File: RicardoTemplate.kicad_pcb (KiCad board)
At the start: 4 copper layers, 42.8 x 63.6 mm, 137 parts, among them IC2 SX1280, J1 RBUS, J2 USB_C_Receptacle_USB2.0, U1 ESP32-S3, U11 SC4215ASTRT, U12 SKY66112-11, U13 DEA202450BT-1213C1, U2 SN65HVD230, U3 LM66200DRLR, U4 MAX77827AEFD+T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

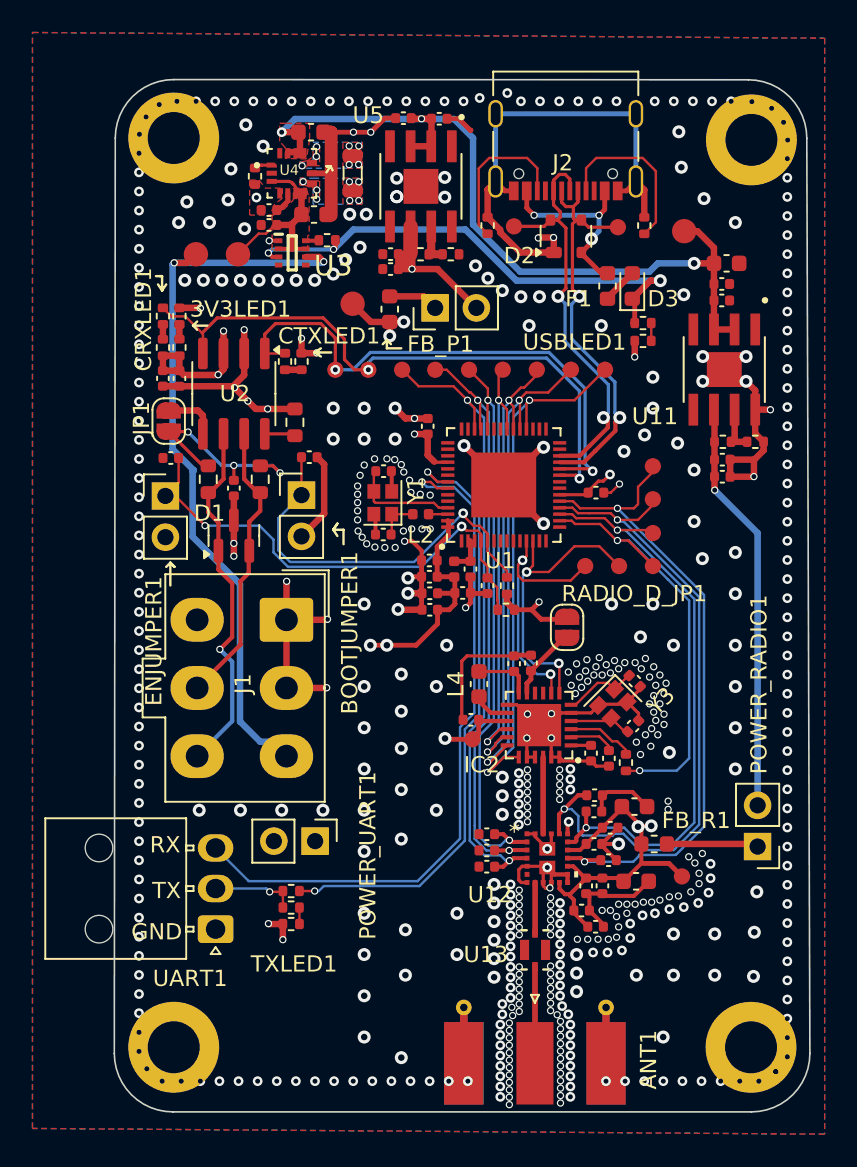
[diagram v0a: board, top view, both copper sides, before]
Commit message: Changed via stitching
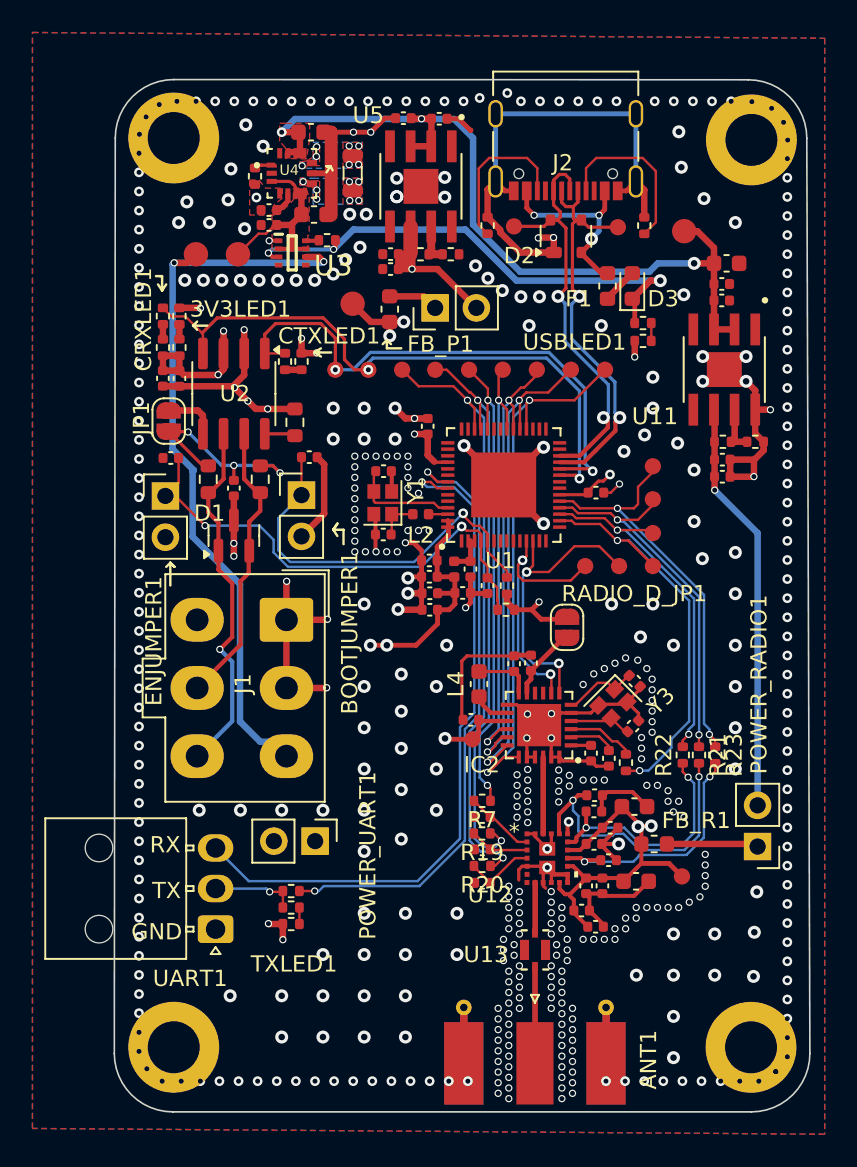
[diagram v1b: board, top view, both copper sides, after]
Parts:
- added R19: 1k, Resistor_SMD:R_0402_1005Metric, F.Cu at (141.1, 117.4)
- added R20: 1k, Resistor_SMD:R_0402_1005Metric, F.Cu at (141.1, 119.4)
- added R21: 1k, Resistor_SMD:R_0402_1005Metric, F.Cu at (154.5, 112.6)
- added R22: 1k, Resistor_SMD:R_0402_1005Metric, F.Cu at (153.5, 112.6)
- added R23: 1k, Resistor_SMD:R_0402_1005Metric, F.Cu at (155.5, 112.6)
- added R7: 1k, Resistor_SMD:R_0402_1005Metric, F.Cu at (141.1, 115.4)
- moved C59 1.09 mm to (141.1, 116.4)
- moved C63 1.03 mm to (141.1, 120.5)
- moved C60 0.28 mm to (141.1, 118.4)
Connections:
- C59 pad 1: CRX -> Net-(U12-CRX)
- C60 pad 1: CSD -> Net-(U12-CSD)
- C63 pad 1: ANT_SEL -> Net-(U12-ANT_SEL)
- C67 pad 1: CPS -> Net-(U12-CPS)
- C69 pad 2: CHL -> Net-(U12-CHL)
- C72 pad 2: CTX -> Net-(U12-CTX)
- U12 pad 15: CPS -> Net-(U12-CPS)
- U12 pad 17: CTX -> Net-(U12-CTX)
- U12 pad 19: CHL -> Net-(U12-CHL)
- U12 pad 2: CRX -> Net-(U12-CRX)
- U12 pad 3: CSD -> Net-(U12-CSD)
- U12 pad 4: ANT_SEL -> Net-(U12-ANT_SEL)
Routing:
- net CHL: track 42.3 -> 23.0 mm
- net Net-(U12-CHL): track 0.00 -> 18.7 mm, vias 0 -> 2
- net CPS: track 39.9 -> 25.0 mm
- net Net-(U12-CPS): track 0.00 -> 14.9 mm, vias 0 -> 2
- net Net-(U12-CTX): track 0.00 -> 14.5 mm, vias 0 -> 2
- net CTX: track 36.7 -> 22.4 mm
- net CRX: track 35.9 -> 29.6 mm
- net Net-(U12-ANT_SEL): track 0.00 -> 4.36 mm
- net Net-(U12-CRX): track 0.00 -> 4.32 mm
- net GND: track 394.3 -> 398.5 mm, vias 537 -> 478
- net Net-(U12-CSD): track 0.00 -> 3.71 mm
- net ANT_SEL: track 39.8 -> 38.1 mm
- net CSD: track 37.4 -> 35.8 mm
- net RF_RST: track 26.8 -> 25.8 mm

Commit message: Minor improvements
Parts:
- removed D3: D, Diode_SMD:D_0603_1608Metric
- added R25: 20-100, Resistor_SMD:R_0402_1005Metric, F.Cu at (145.0, 90.9)
- added R26: 20-100, Resistor_SMD:R_0402_1005Metric, F.Cu at (144.0, 90.9)
- added R29: 20-100, Resistor_SMD:R_0402_1005Metric, F.Cu at (143.0, 90.9)
- added R30: 20-100, Resistor_SMD:R_0402_1005Metric, F.Cu at (142.0, 90.9)
- added R31: 20-100, Resistor_SMD:R_0402_1005Metric, F.Cu at (139.8, 114.5)
- added R32: 20-100, Resistor_SMD:R_0402_1005Metric, F.Cu at (139.8, 113.2)
- added R33: 20-100, Resistor_SMD:R_0402_1005Metric, F.Cu at (139.8, 112.0)
- added R34: 20-100, Resistor_SMD:R_0402_1005Metric, F.Cu at (139.8, 111.0)
- moved BBOUT_TP1 27.4 mm to (126.8, 74.4)
- moved R28 20.2 mm to (151.9, 74.0), turned to 90 degrees
- moved C64 19.7 mm to (152.9, 75.9), turned to -90 degrees
- moved R27 17.8 mm to (151.9, 75.9), turned to 90 degrees
- moved C62 17.1 mm to (151.9, 77.8), turned to 90 degrees
- moved C19 15.9 mm to (143.4, 74.7), turned to 90 degrees
- moved U11 15.4 mm to (147.7, 75.9), turned to 0 degrees
- moved C12 15.2 mm to (142.0, 76.9), turned to -90 degrees
- moved J2 14.2 mm to (156.8, 84.8), turned to 90 degrees
- moved C18 14.1 mm to (143.4, 77.1), turned to -90 degrees
- moved R12 10.7 mm to (152.1, 80.0), turned to 180 degrees
- moved R11 9.76 mm to (152.1, 89.7), turned to 0 degrees
- moved D+_TP1 9.13 mm to (152.1, 81.7), turned to -90 degrees
- moved D-_TP1 8.37 mm to (152.0, 88.1), turned to -90 degrees
- moved R13 6.77 mm to (153.6, 92.2), turned to 90 degrees
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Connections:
- F1 pad 2: Net-(D3-A) -> VBUS
- IC2 pad 16: MISO -> Net-(IC2-MISO_TX)
- IC2 pad 17: MOSI -> Net-(IC2-MOSI_RX)
- IC2 pad 18: SCK -> Net-(IC2-SCK_RTSN)
- IC2 pad 19: CS -> Net-(IC2-NSS_CTS)
- U1 pad 32: CS -> Net-(U1-SPICS0/GPIO29)
- U1 pad 33: SCK -> Net-(U1-SPICLK/GPIO30)
- U1 pad 34: MOSI -> Net-(U1-SPIQ/GPIO31)
- U1 pad 35: MISO -> Net-(U1-SPID/GPIO32)
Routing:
- net Net-(POWER_RADIO1-Pin_2): track 25.5 -> 45.6 mm
- net +VDC: track 50.0 -> 32.9 mm
- net GND: track 398.5 -> 382.4 mm, vias 478 -> 178
- net VBUS: track 31.3 -> 39.2 mm
- net /RXD: track 43.4 -> 36.6 mm
- net Net-(U1-U0TXD/PROG/GPIO43): track 38.0 -> 31.7 mm
- net /CHIP_PU: track 30.7 -> 36.5 mm
- net CRX: track 29.6 -> 34.3 mm
- net Net-(IC2-NSS_CTS): track 0.00 -> 3.92 mm
- net ANT_SEL: track 38.1 -> 42.0 mm
- net DIO1: track 16.6 -> 12.8 mm
- net /Data-: track 25.3 -> 21.5 mm
- net CSD: track 35.8 -> 39.4 mm
- net Net-(IC2-SCK_RTSN): track 0.00 -> 3.13 mm
- net /Data+: track 25.9 -> 22.9 mm
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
